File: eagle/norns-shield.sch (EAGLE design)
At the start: 77 parts, among them J1 TRS-IN, J2 TRS-OUT, J3 ISP-ROW, Q1 ASFL-12.288mhz, SW1 PVA1, SW2 PVA1, SW3 PVA1, U1 CS4270, X1 RASPI_BOARD_B+#_E3

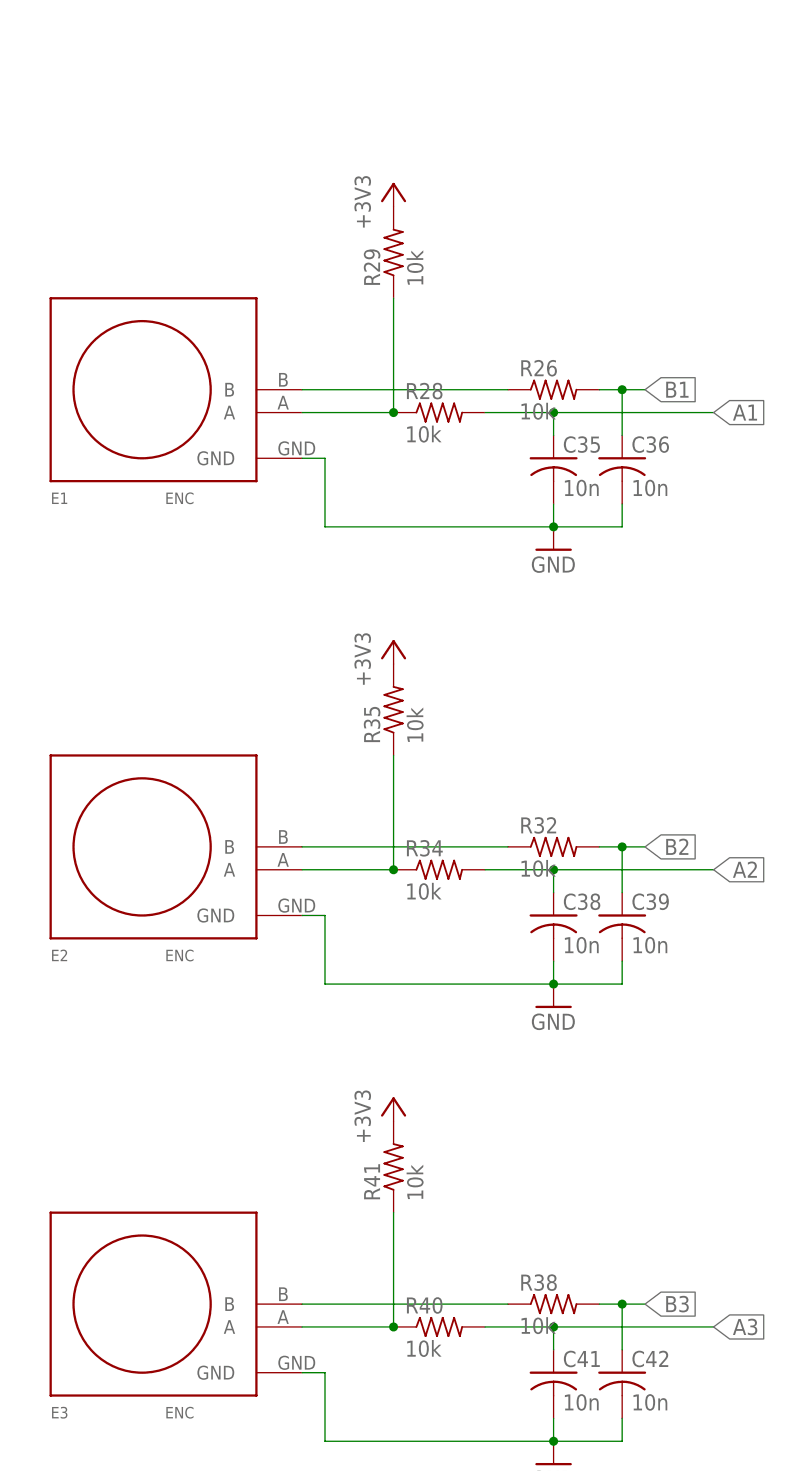
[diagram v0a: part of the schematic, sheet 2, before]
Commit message: 191021, add pullups to encoders
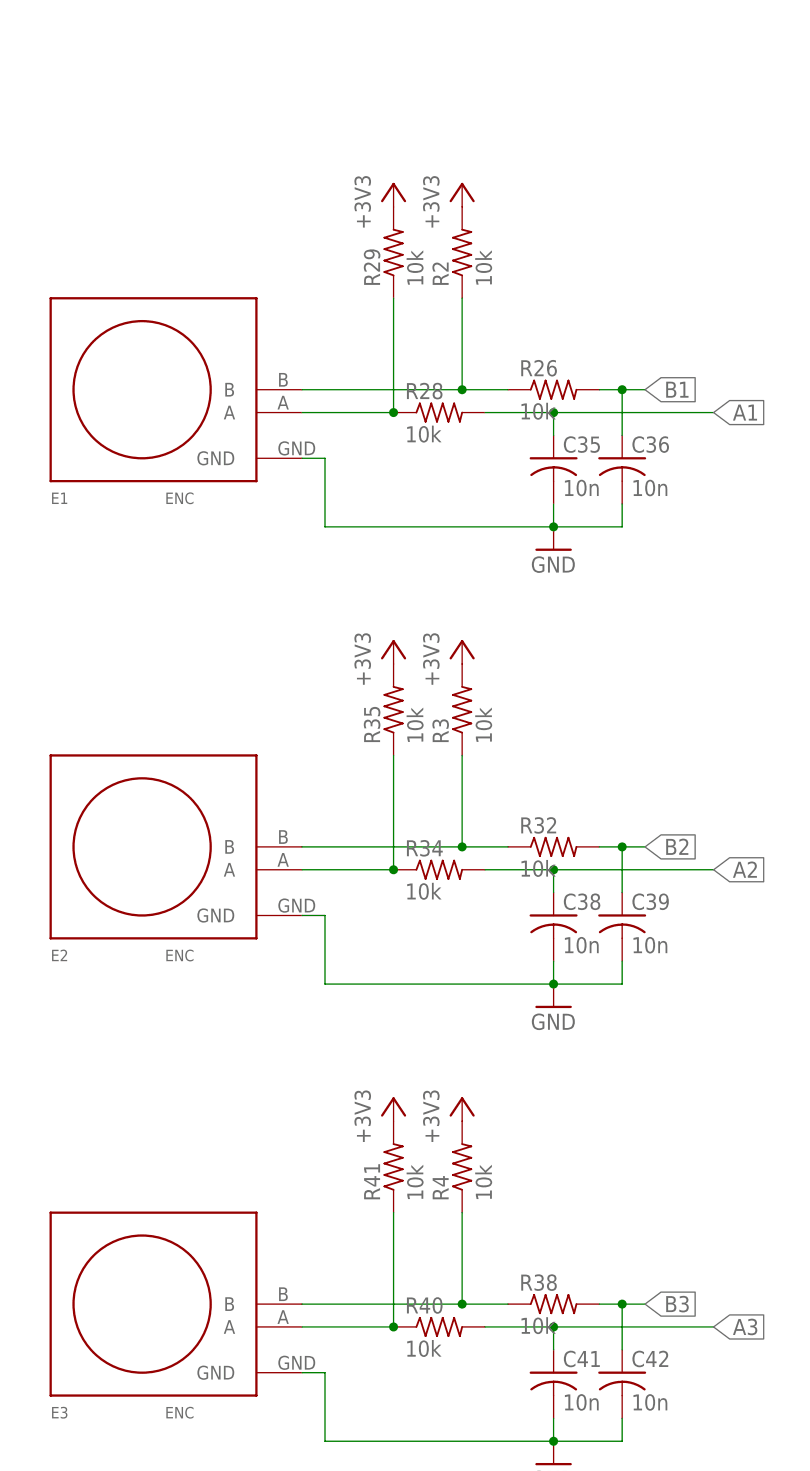
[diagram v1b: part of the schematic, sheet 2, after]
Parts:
- added R2, R3, R4: 10k, rcl:R-US_R0603
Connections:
- net +3V3: now also R2.2, R3.2, R4.2
- net N$19: now also R2.1
- net N$22: now also R3.1
- net N$27: now also R4.1
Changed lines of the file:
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@@
 <part name="E3" library="lines" deviceset="ENC" device=""/>
 <part name="J3" library="monome-inc" deviceset="ISP-ROW" device=""/>
+<part name="R2" library="rcl" deviceset="R-US_" device="R0603" value="10k"/>
+<part name="+3V12" library="supply1" deviceset="+3V3" device=""/>
+<part name="R3" library="rcl" deviceset="R-US_" device="R0603" value="10k"/>
+<part name="+3V13" library="supply1" deviceset="+3V3" device=""/>
+<part name="R4" library="rcl" deviceset="R-US_" device="R0603" value="10k"/>
+<part name="+3V14" library="supply1" deviceset="+3V3" device=""/>
 </parts>
 <sheets>
@@
 <instance part="E2" gate="G$1" x="93.98" y="119.38"/>
 <instance part="E3" gate="G$1" x="93.98" y="68.58"/>
+<instance part="R2" gate="G$1" x="129.54" y="185.42" rot="R90"/>
+<instance part="+3V12" gate="G$1" x="129.54" y="193.04"/>
+<instance part="R3" gate="G$1" x="129.54" y="134.62" rot="R90"/>
+<instance part="+3V13" gate="G$1" x="129.54" y="142.24"/>
+<instance part="R4" gate="G$1" x="129.54" y="83.82" rot="R90"/>
+<instance part="+3V14" gate="G$1" x="129.54" y="91.44"/>
 </instances>
 <busses>
@@
 <segment>
 <pinref part="R26" gate="G$1" pin="1"/>
-<wire x1="111.76" y1="170.18" x2="134.62" y2="170.18" width="0.1524" layer="91"/>
+<wire x1="111.76" y1="170.18" x2="129.54" y2="170.18" width="0.1524" layer="91"/>
 <pinref part="E1" gate="G$1" pin="B"/>
+<pinref part="R2" gate="G$1" pin="1"/>
+<wire x1="129.54" y1="170.18" x2="134.62" y2="170.18" width="0.1524" layer="91"/>
+<wire x1="129.54" y1="180.34" x2="129.54" y2="170.18" width="0.1524" layer="91"/>
+<junction x="129.54" y="170.18"/>
 </segment>
 </net>
@@
 <segment>
 <pinref part="R32" gate="G$1" pin="1"/>
-<wire x1="111.76" y1="119.38" x2="134.62" y2="119.38" width="0.1524" layer="91"/>
+<wire x1="111.76" y1="119.38" x2="129.54" y2="119.38" width="0.1524" layer="91"/>
 <pinref part="E2" gate="G$1" pin="B"/>
+<pinref part="R3" gate="G$1" pin="1"/>
+<wire x1="129.54" y1="119.38" x2="134.62" y2="119.38" width="0.1524" layer="91"/>
+<wire x1="129.54" y1="129.54" x2="129.54" y2="119.38" width="0.1524" layer="91"/>
+<junction x="129.54" y="119.38"/>
 </segment>
 </net>
@@
 <segment>
 <pinref part="R38" gate="G$1" pin="1"/>
-<wire x1="111.76" y1="68.58" x2="134.62" y2="68.58" width="0.1524" layer="91"/>
+<wire x1="111.76" y1="68.58" x2="129.54" y2="68.58" width="0.1524" layer="91"/>
 <pinref part="E3" gate="G$1" pin="B"/>
+<pinref part="R4" gate="G$1" pin="1"/>
+<wire x1="129.54" y1="68.58" x2="134.62" y2="68.58" width="0.1524" layer="91"/>
+<wire x1="129.54" y1="68.58" x2="129.54" y2="78.74" width="0.1524" layer="91"/>
+<junction x="129.54" y="68.58"/>
 </segment>
 </net>
@@
 <pinref part="+3V8" gate="G$1" pin="+3V3"/>
 </segment>
-</net>
+<segment>
+<pinref part="R2" gate="G$1" pin="2"/>
+<pinref part="+3V12" gate="G$1" pin="+3V3"/>
+</segment>
+<segment>
+<pinref part="R3" gate="G$1" pin="2"/>
+<pinref part="+3V13" gate="G$1" pin="+3V3"/>
+</segment>
+<segment>
+<pinref part="R4" gate="G$1" pin="2"/>
+<pinref part="+3V14" gate="G$1" pin="+3V3"/>
+</segment>
+</net>
